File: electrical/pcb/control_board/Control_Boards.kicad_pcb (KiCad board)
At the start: 2 copper layers, 181.6 x 252.8 mm, 118 parts, among them J1 XT30-M, J10 Molex_172675-0613, J11 Molex_172675-0613, J12 TSW-104-07-F-T, J13 Molex_172675-0613, J14 Molex_172675-0613, J15 TSW-104-07-F-T, J16 277-11404-ND, J17 277-11404-ND, J18 277-11404-ND, J19 TSW-104-07-F-T, J2 XT30-F, J20 PEC08SAAN, J21 PPTC102LFBN-RC, J22 S9175-ND_rpi_breakout, J23 S9175-ND_rpi_breakout, J24 6posheader, J25 SSW-104-01-F-T, J26 WM6548-ND, J27 PPTC021LFBN-RC, J28 PPTC021LFBN-RC, J29 PPTC021LFBN-RC, J3 XT30-F, J4 XT30-F, J5 XT30-M, J6 ED2580-ND, J7 TSW-104-07-F-T, J8 Molex_172675-0613, J9 Molex_172675-0613, M1 Mounting_Holes, Q1 2N3906, Q2 2N3906, Q3 2N3906, SW1 CT206124-ND, T1 test_point, T2 test_point, T3 test_point, T4 test_point, T5 test_point, U1 INA260, U2 PCA9685, U3 D24V22Fx, U4 D24V150Fx, U5 DC7G3HWA, U6 DC7G3HWA, y1 rover_silkscreen

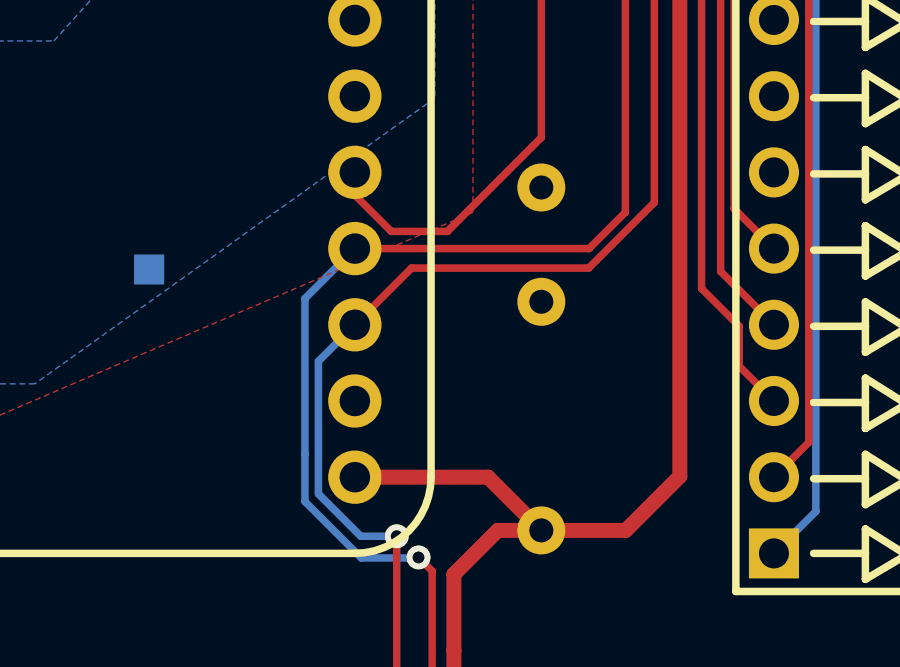
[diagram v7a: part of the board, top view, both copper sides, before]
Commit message: Moved alert from pull-down to +3.3V pull-up
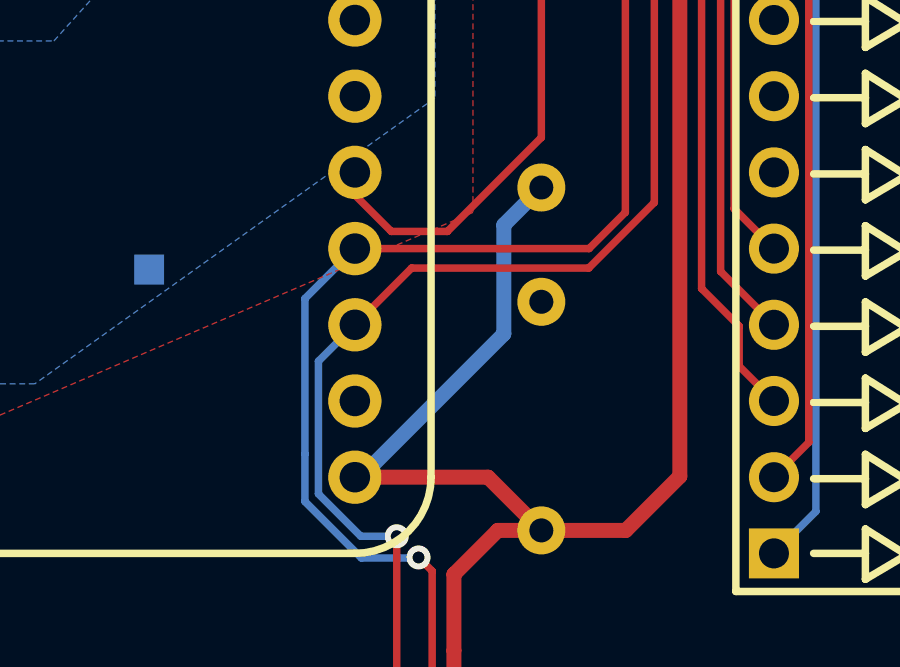
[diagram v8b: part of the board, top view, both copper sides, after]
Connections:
- R5 pad 1: GND_motor -> +3.3V_motor
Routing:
- net +3.3V_motor: track 250.5 -> 262.8 mm
